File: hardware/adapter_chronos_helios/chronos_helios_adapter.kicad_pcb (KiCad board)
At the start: 4 copper layers, 28 x 25 mm, 11 parts, among them J1 FPC-05F-22PH20, J2 FPC-05F-22PH20

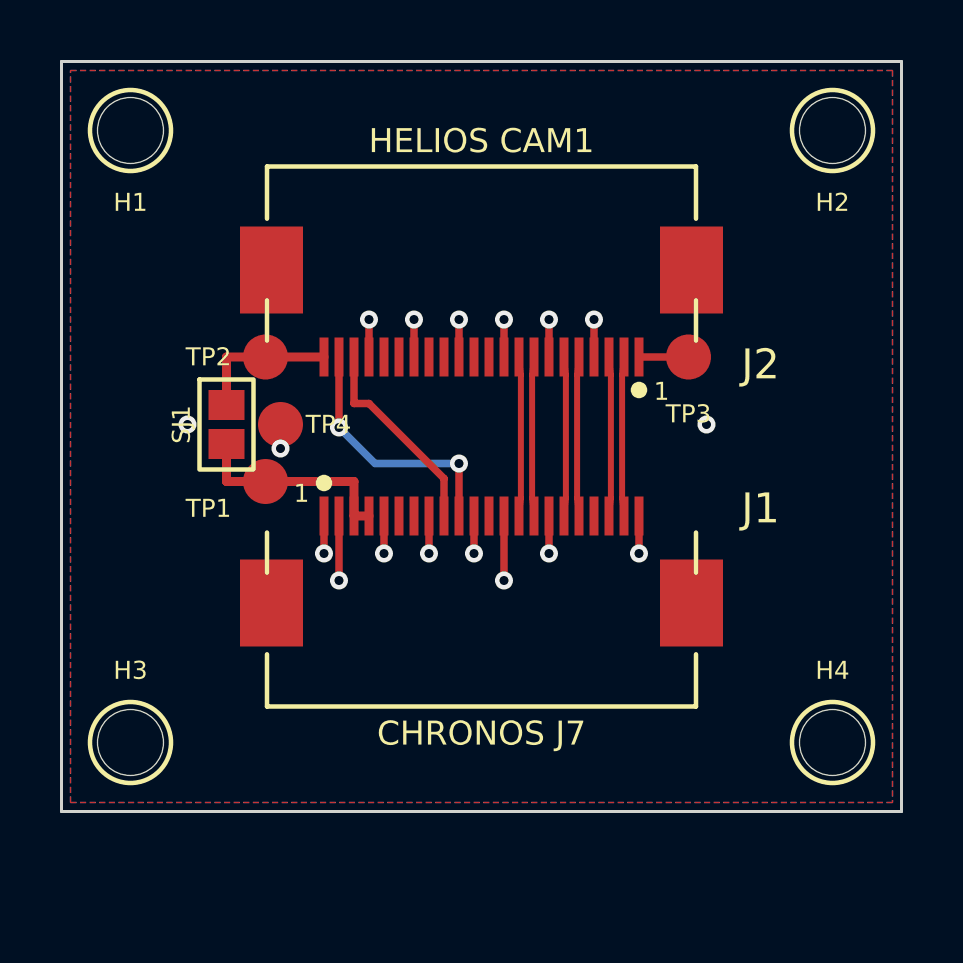
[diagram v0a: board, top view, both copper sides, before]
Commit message: hardware: adapter v2 - native 15p Helios side, crossover routed on board
J2 changed from 22p RPi-mapped to a native 15-pin FH12 (XFCN F0502-B-15-15T-R, LCSC C2844857) so both cables are plain straight Type-A FFCs (Aerium 15p-22p cable no longer needed). Pin-1 sides differ between the boards, so the full pin-order reversal + I2C swap is routed inside the adapter: In2.Cu crossover lanes over a solid B.Cu GND plane, staggered 0.5/0.3 vias, I2C C-detour on the east side. Board grown to 28x28mm for the crossover field. DRC: 0 errors, 0 unconnected. Fab outputs, BOM/CPL, renders and README regenerated.
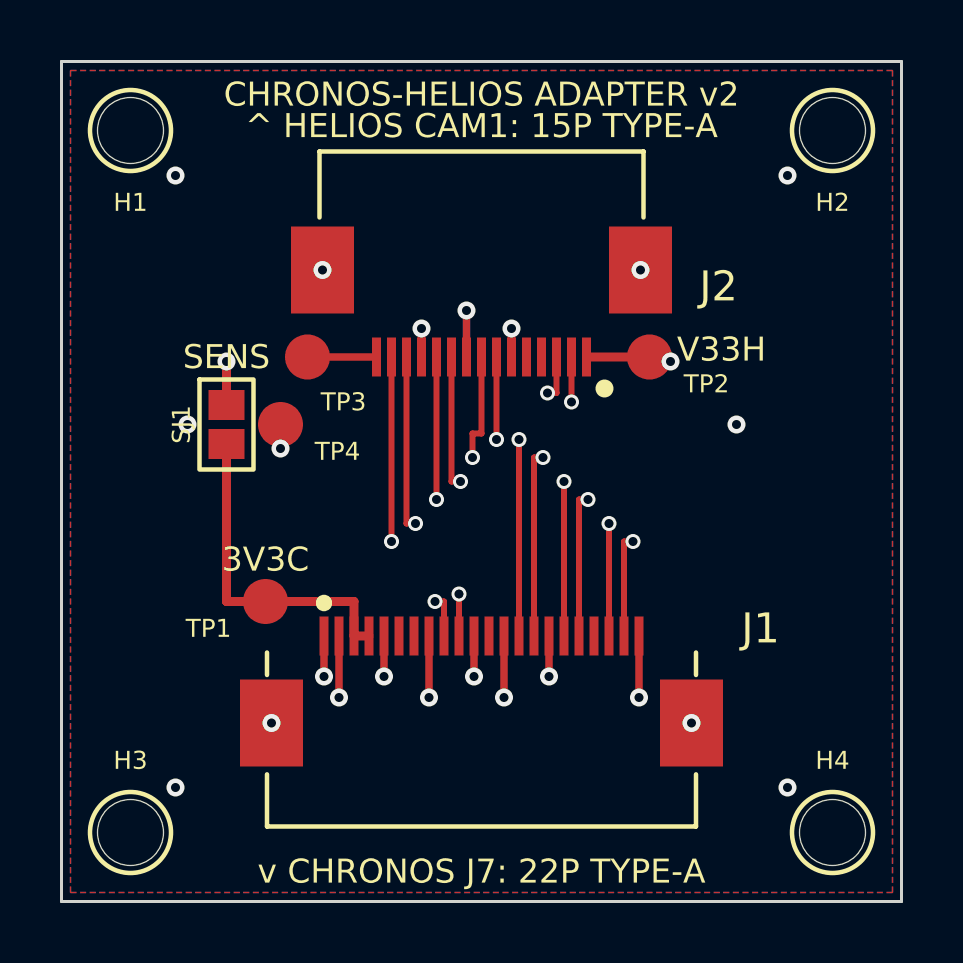
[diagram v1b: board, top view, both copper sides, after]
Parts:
- J2: value FPC-05F-22PH20 -> F0502-B-15-15T-R; footprint Connector_FFC-FPC:Hirose_FH12-22S-0.5SH_1x22-1MP_P0.50mm_Horizontal -> Connector_FFC-FPC:Hirose_FH12-15S-0.5SH_1x15-1MP_P0.50mm_Horizontal
- moved TP2 12.8 mm to (117.6, 107.8)
- moved TP3 12.7 mm to (106.2, 107.8)
- moved J1 4.00 mm to (112.0, 119.0)
- moved TP1 4.00 mm to (104.8, 116.0)
- moved H3 3.00 mm to (100.3, 123.7)
- moved H4 3.00 mm to (123.7, 123.7)
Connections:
- J2 pad 1: SENSE_H -> V33_HELIOS
- J2 pad 10: GND -> CSI_D1_P
- J2 pad 11: (no net) -> CSI_D1_N
- J2 pad 12: (no net) -> GND
- J2 pad 13: GND -> CSI_D0_P
- J2 pad 14: (no net) -> CSI_D0_N
- J2 pad 15: (no net) -> SENSE_H
- J2 pad 2: CSI_D0_N -> I2C_SDA
- J2 pad 3: CSI_D0_P -> I2C_SCL
- J2 pad 4: GND -> (no net)
- J2 pad 5: CSI_D1_N -> (no net)
- J2 pad 6: CSI_D1_P -> GND
- J2 pad 7: GND -> CSI_CLK_P
- J2 pad 9: CSI_CLK_P -> GND
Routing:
- net I2C_SCL: track 6.84 -> 24.4 mm, vias 0 -> 2
- net V33_HELIOS: track 4.85 -> 19.2 mm, vias 0 -> 2
- net CSI_D0_N: track 5.31 -> 17.7 mm, vias 0 -> 2
- net I2C_SDA: track 8.60 -> 19.9 mm
- net CSI_D0_P: track 5.31 -> 16.1 mm, vias 0 -> 2
- net CSI_D1_N: track 5.31 -> 14.7 mm, vias 0 -> 2
- net CSI_D1_P: track 5.31 -> 13.1 mm, vias 0 -> 2
- net CSI_CLK_N: track 5.31 -> 12.2 mm, vias 0 -> 2
- net CSI_CLK_P: track 5.31 -> 10.1 mm, vias 0 -> 2
- net V33_CHRONOS: track 7.15 -> 11.2 mm
- net GND: track 20.1 -> 17.8 mm, vias 17 -> 22
- net SENSE_H: track 1.65 -> 2.30 mm
- removed copper zone on In2.Cu, net GND
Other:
- board size 28 x 25 mm -> 28 x 28 mm
- board text added: "3V3C"
- board text added: "BEFORE POWER:"
- board text added: "BOTH CABLES: STRAIGHT TYPE-A FFC"
- board text added: "CHRONOS-HELIOS ADAPTER v2"
- board text added: "CROSSOVER ON BOARD"
- board text added: "SENS"
- board text added: "SJ1 OPEN = 3V3 RAILS ISOLATED"
- board text added: "TP-V33H=3.3V, TP-SENS=GND"
- board text added: "V33H"
- board text added: "^ HELIOS CAM1: 15P TYPE-A"
- board text added: "v CHRONOS J7: 22P TYPE-A"
- board text removed: "1"
- board text removed: "CHRONOS J7"
- board text removed: "CHRONOS J7 <-> HELIOS CAM1 ADAPTER v1 J1: straight 22p 0.5mm Type-A FFC to Chronos J7 J2: Aerium 15p-22p FORWARD cable, 22p end here SJ1 OPEN = supplies isolated (default) Check TP1=3.3V (Chronos on) and TP2=3.3V, TP3=GND (Helios on) BEFORE full hookup. Wrong reading = swap cable polarity type."
- board text removed: "HELIOS CAM1"
